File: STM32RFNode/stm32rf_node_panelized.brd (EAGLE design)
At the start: 57.1 x 17.8 mm, 7 parts, among them X1 USB-A-H

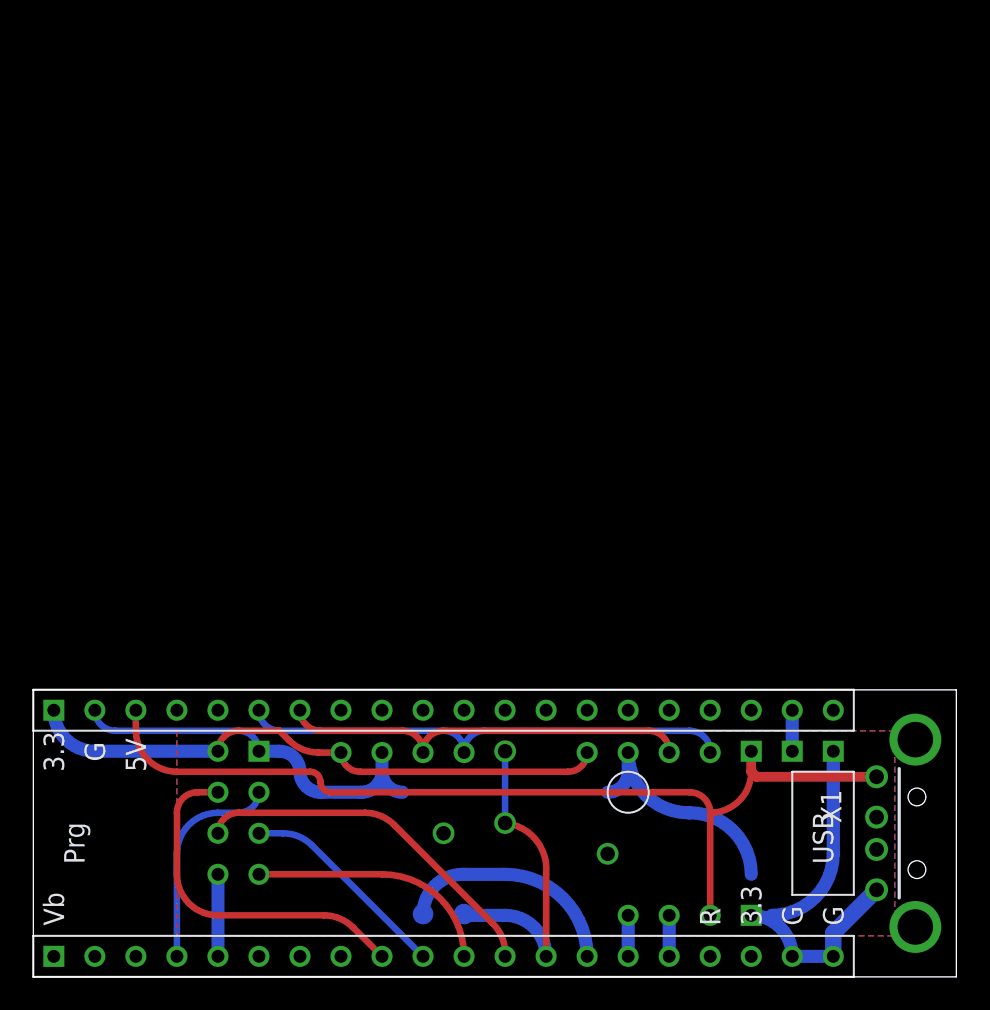
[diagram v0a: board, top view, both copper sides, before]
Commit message: new production with usb connector
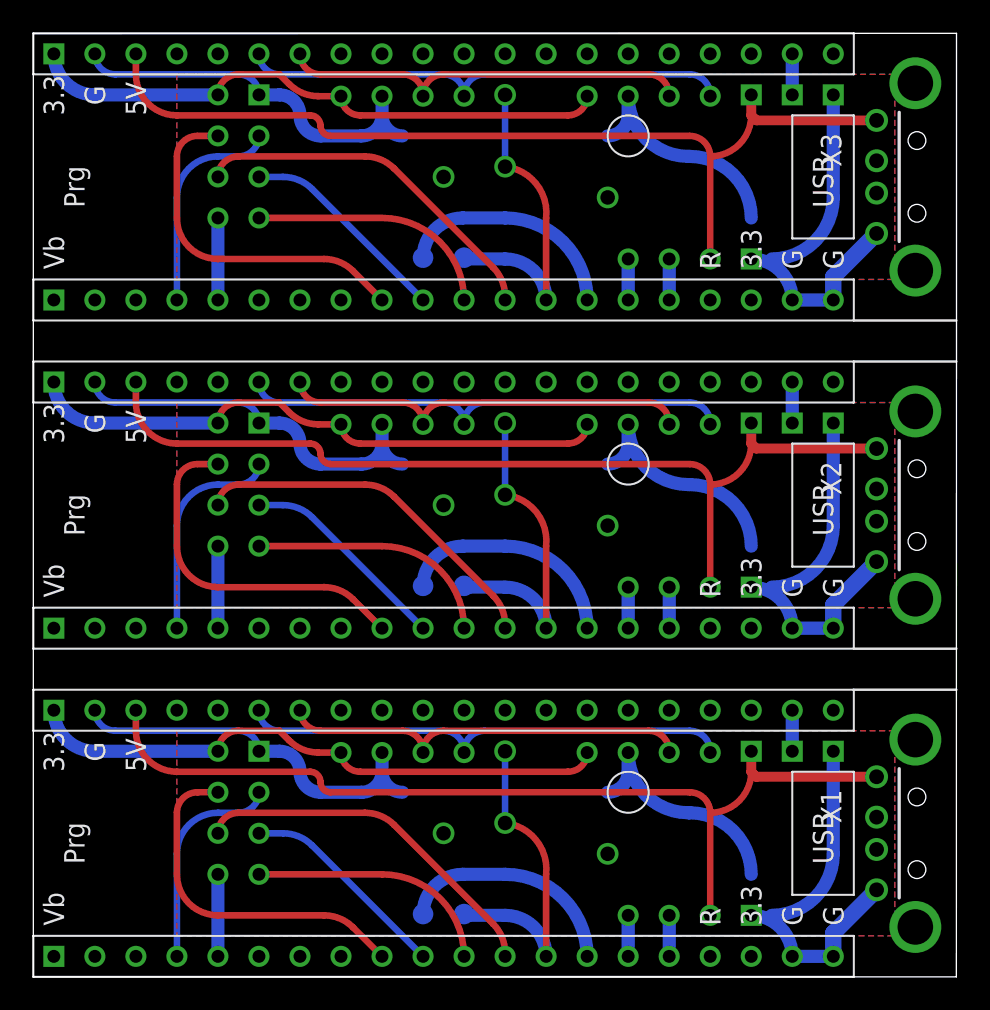
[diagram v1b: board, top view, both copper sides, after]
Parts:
- added U$10, U$16: GY-49G-49-SURF, GY-49:GY-49-SURF
- added U$11, U$17: ONE_WIRE'RIGHT', one-wire:ONE_WIRE_RIGHT
- added U$12, U$18: UARTMINI, WFConnectors:UART-MINI
- added U$13, U$7: STM32_BLUEPILL, stm32_bluepill:STM32_BLUEPILL
- added U$14, U$8: NRF24L01+REFDESIGNMINI, nRF24L01+RefDesign:NRF24L01+REFDESIGN-MINI
- added U$15, U$9: GY-BMEPGY-BMEP-NOHOLE, GY-BMEP:GY-BMEP-NOHOLE
- added X2, X3: USB-A-H, usb:USB-A-H
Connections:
- new net 3V1: U$10.VIN, U$7.3V3@2, U$8.2, U$9.VIN
- new net 3V2: U$13.3V3@2, U$14.2, U$15.VIN, U$16.VIN
- new net 5V1: U$11.5V, U$12.2, U$7.5V, X2.VBUS
- new net 5V2: U$13.5V, U$17.5V, U$18.2, X3.VBUS
- new net GND1: U$10.GND, U$11.GND, U$12.1, U$7.GND@1, U$7.GND@2, U$7.GND@3, U$8.1, U$9.GND, X2.GND
- new net GND2: U$13.GND@1, U$13.GND@2, U$13.GND@3, U$14.1, U$15.GND, U$16.GND, U$17.GND, U$18.1, X3.GND
- new net INT1: U$10.INT, U$7.PB_0
- new net INT2: U$13.PB_0, U$16.INT
- new net N$13: U$12.4, U$7.PB_10
- new net N$14: U$12.3, U$7.PB_11
- new net N$15: U$10.SCL, U$7.PB_6, U$9.SCL
- new net N$16: U$10.SDA, U$7.PB_7, U$9.SDA
- new net N$17: U$7.PA_7, U$8.6
- new net N$18: U$7.PA_6, U$8.7
- new net N$19: U$7.PA_5, U$8.5
- new net N$20: U$7.PA_4, U$8.4
- new net N$21: U$10.A0, U$7.PB_1
- new net N$22: U$7.PA_0, U$8.8
- new net N$23: U$7.PC_15, U$8.3
- new net N$24: U$11.S, U$7.PB_13
- new net N$25: U$13.PB_10, U$18.4
- new net N$26: U$13.PB_11, U$18.3
- new net N$27: U$13.PB_6, U$15.SCL, U$16.SCL
- new net N$28: U$13.PB_7, U$15.SDA, U$16.SDA
- new net N$29: U$13.PA_7, U$14.6
- new net N$30: U$13.PA_6, U$14.7
- new net N$31: U$13.PA_5, U$14.5
- new net N$32: U$13.PA_4, U$14.4
- new net N$33: U$13.PB_1, U$16.A0
- new net N$34: U$13.PA_0, U$14.8
- new net N$35: U$13.PC_15, U$14.3
- new net N$36: U$13.PB_13, U$17.S
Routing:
- net GND2: track 0.00 -> 60.2 mm, vias 0 -> 2
- net GND1: track 0.00 -> 60.2 mm, vias 0 -> 2
- net 5V1: track 0.00 -> 58.0 mm
- net 5V2: track 0.00 -> 58.0 mm
- net 3V2: track 0.00 -> 36.0 mm
- net 3V1: track 0.00 -> 36.0 mm
- net N$28: track 0.00 -> 30.3 mm
- net N$16: track 0.00 -> 30.3 mm
- net N$27: track 0.00 -> 25.2 mm
- net N$15: track 0.00 -> 25.2 mm
- net N$17: track 0.00 -> 22.4 mm
- net N$29: track 0.00 -> 22.4 mm
- net N$32: track 0.00 -> 21.5 mm
- net N$20: track 0.00 -> 21.5 mm
- net INT2: track 0.00 -> 19.8 mm, vias 0 -> 2
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- added copper zone on layer 1, net GND1
- added copper zone on layer 16, net GND1
- added copper zone on layer 1, net GND2
- added copper zone on layer 16, net GND2
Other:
- board size 57.1 x 17.8 mm -> 57.2 x 58.4 mm
